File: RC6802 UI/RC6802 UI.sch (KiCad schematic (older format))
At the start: 71 parts, among them J1 TAPE, J2 RC6802_UI_Port, M1 Mounting, M2 Mounting, M3 Mounting, M4 Mounting, Q1 2N3904, Q2 2N3904, Q3 2N3904, Q4 2N3904, Q5 2N3904, SW1 RESET, SW10 D, SW11 2, SW12 6, SW13 A, SW14 E, SW15 3, SW16 7, SW17 B, SW18 F, SW19 LOAD, SW2 SST, SW3 Ø, SW4 4, SW5 8, SW6 C, SW7 1, SW8 5, SW9 9, U1 74LS374, U2 74LS00

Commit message: Assigned 7segment and tape footprints
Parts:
- added C3: 100nF, Capacitors_THT:C_Disc_D4.7mm_W2.5mm_P5.00mm, symbol C
- added SW20: STEP, symbol SW_SPDT
- AFF1, AFF2: footprint (none) -> Displays_7-Segment:7SegmentLED_LTS6760_LTS6780
- D1: footprint (none) -> LEDs:LED_D5.0mm
- D2, D3, D4: footprint (none) -> Diodes_THT:D_DO-35_SOD27_P7.62mm_Horizontal
- J1: footprint (none) -> TRS:Tayda_3.5mm_stereo_TRS_jack_A-853
- R1, R10, R11, R12, R13, R14, R15, R16, R17, R18, R19, R2, R20, R21, R22, R23, R24, R25, R26, R3, R4, R5, R6, R7, R8, R9: footprint (none) -> Resistors_THT:R_Axial_DIN0207_L6.3mm_D2.5mm_P10.16mm_Horizontal
- SW1, SW10, SW11, SW12, SW13, SW14, SW15, SW16, SW17, SW18, SW3, SW4, SW5, SW6, SW7, SW8, SW9: footprint (none) -> Buttons_Switches_THT:SW_PUSH_6mm
- SW19, SW2: footprint (none) -> Pin_Headers:Pin_Header_Straight_1x03_Pitch2.54mm
- U1: footprint (none) -> Housings_DIP:DIP-20_W7.62mm_Socket
- U2: footprint (none) -> Housings_DIP:DIP-14_W7.62mm_Socket
- renumbered C3 to C8
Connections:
- wire segments 233 -> 235
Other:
- note added: "Uses the same cable setup as found\non the ZX Spectrum +3, with EAR\nis data from tape to computer -\nMIC is data out to tape."

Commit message: UI board layout done
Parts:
- removed Q1, Q2: 2N3904, TO_SOT_Packages_THT:TO-92_Molded_Narrow, symbol 2N3904
- removed SW19: LOAD, Pin_Headers:Pin_Header_Straight_1x03_Pitch2.54mm, symbol SW_SPDT
- removed SW2: SST, Pin_Headers:Pin_Header_Straight_1x03_Pitch2.54mm, symbol SW_SPDT
- removed SW20: STEP, symbol SW_SPDT
- added J3: EXT_KEYPAD, Pin_Headers:Pin_Header_Angled_2x05_Pitch2.54mm, symbol Conn_02x05_Odd_Even
- added Q1, Q2: 2N3906, TO_SOT_Packages_THT:TO-92_Molded_Narrow, symbol 2N3906
- added R27, R29: 220, Resistors_THT:R_Axial_DIN0207_L6.3mm_D2.5mm_P10.16mm_Horizontal, symbol R
- added R28, R30: 1k, Resistors_THT:R_Axial_DIN0207_L6.3mm_D2.5mm_P10.16mm_Horizontal, symbol R
- added SW19: TAPE, DPDT_Switch:dpdt_switch, symbol SW_DPDT_x2
- added SW2: SW_SST, DPDT_Switch:dpdt_switch, symbol SW_DPDT_x2
- added SW20: STEP, DPDT_Switch:dpdt_switch, symbol SW_DPDT_x2
- added SW21: HW_SST, DPDT_Switch:dpdt_switch, symbol SW_DPDT_x2
- added U3: 74LS73, Housings_DIP:DIP-14_W7.62mm_Socket, symbol 74LS73
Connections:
- net labels added: E, ~HALT
- wire segments 235 -> 278
- no-connect marks 20 -> 31
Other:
- note added: "RC6802 Microchicken computer as explained in the book "22 Micro-computer projects:\nTo build, use and learn" by Daniel Metzger. UI board implements 7segment output, tape\ninput/output, single-step circuit and keypad.\n\nComponents for keypad (in favor of an external one), tape and the 74LS73 (for SST) can\nbe left out if not needed."
- note added: "Software SST is used by latching\nthe IRQ line permanently low."
- moved on the sheet: AFF1, AFF2, C1, C2, C3, C4, C5, C6, C7, C8, D1, D2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

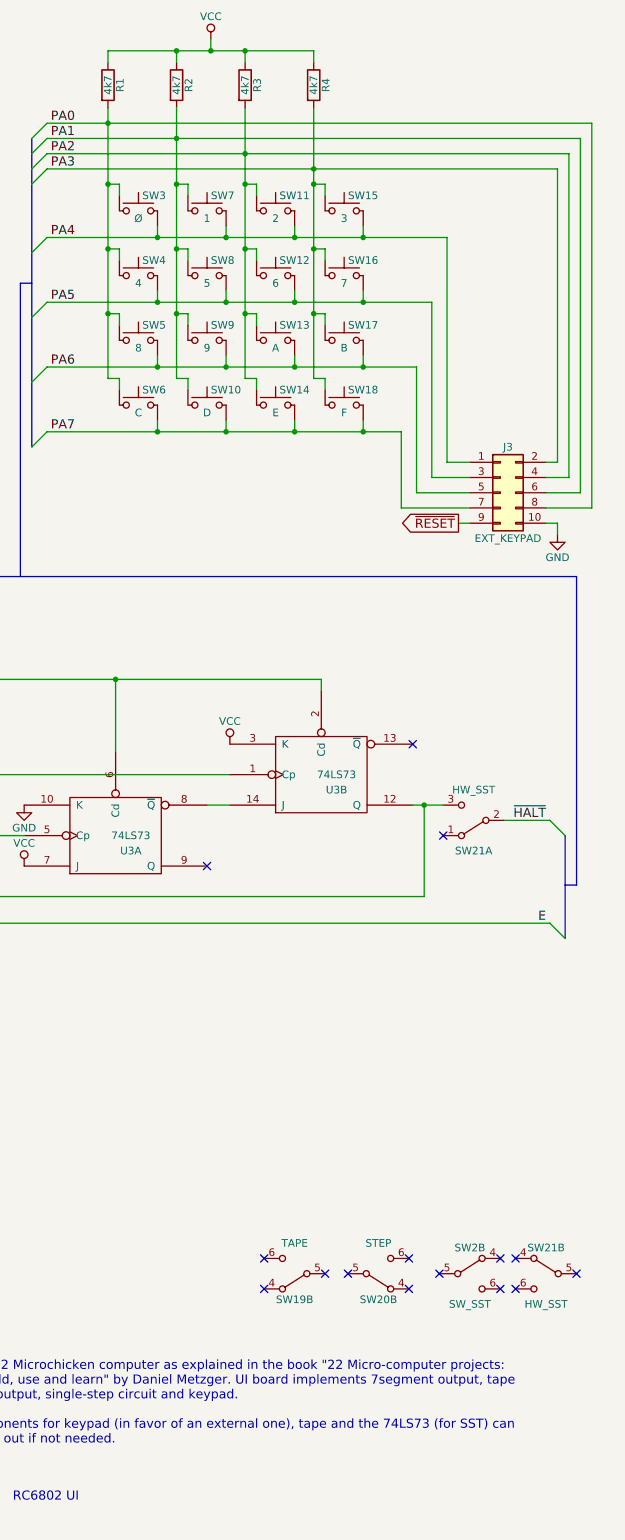
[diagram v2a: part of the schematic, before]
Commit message: Updated UI to change footprints
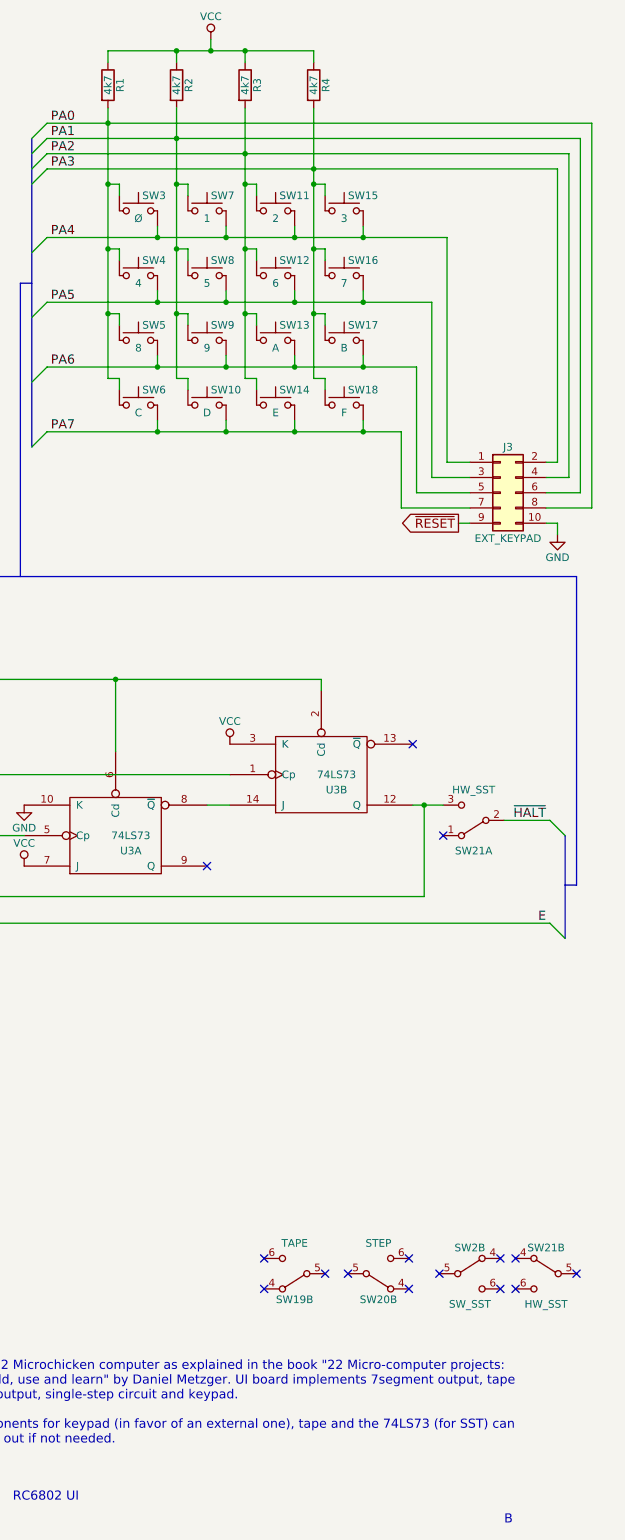
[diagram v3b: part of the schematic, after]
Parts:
- SW19, SW2, SW20, SW21: footprint DPDT_Switch:dpdt_switch -> DPDT_Switch:dpdt_switch_black
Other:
- note added: "B"
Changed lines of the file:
@@
 $EndComp
 $Comp
-L GND #PWR6
+L GND #PWR01
 U 1 1 5D65DEF6
 P 3325 1700
-F 0 "#PWR6" H 3325 1450 50  0001 C CNN
+F 0 "#PWR01" H 3325 1450 50  0001 C CNN
 F 1 "GND" H 3325 1550 50  0000 C CNN
 F 2 "" H 3325 1700 50  0001 C CNN
@@
 $EndComp
 $Comp
-L VCC #PWR1
+L VCC #PWR02
 U 1 1 5D65E216
 P 1825 1550
-F 0 "#PWR1" H 1825 1400 50  0001 C CNN
+F 0 "#PWR02" H 1825 1400 50  0001 C CNN
 F 1 "VCC" H 1825 1700 50  0000 C CNN
 F 2 "" H 1825 1550 50  0001 C CNN
@@
 $EndComp
 $Comp
-L GND #PWR19
+L GND #PWR03
 U 1 1 5D71E74B
 P 11475 10875
-F 0 "#PWR19" H 11475 10625 50  0001 C CNN
+F 0 "#PWR03" H 11475 10625 50  0001 C CNN
 F 1 "GND" H 11475 10725 50  0000 C CNN
 F 2 "" H 11475 10875 50  0001 C CNN
@@
 $EndComp
 $Comp
-L VCC #PWR18
+L VCC #PWR04
 U 1 1 5D72035A
 P 10875 10275
-F 0 "#PWR18" H 10875 10125 50  0001 C CNN
+F 0 "#PWR04" H 10875 10125 50  0001 C CNN
 F 1 "VCC" H 10875 10425 50  0000 C CNN
 F 2 "" H 10875 10275 50  0001 C CNN
@@
 $EndComp
 $Comp
-L GND #PWR5
+L GND #PWR05
 U 1 1 5D72A34D
 P 2925 3600
-F 0 "#PWR5" H 2925 3350 50  0001 C CNN
+F 0 "#PWR05" H 2925 3350 50  0001 C CNN
 F 1 "GND" H 2925 3450 50  0000 C CNN
 F 2 "" H 2925 3600 50  0001 C CNN
@@
 ~RESET
 $Comp
-L GND #PWR3
+L GND #PWR06
 U 1 1 5D840F7E
 P 2000 4450
-F 0 "#PWR3" H 2000 4200 50  0001 C CNN
+F 0 "#PWR06" H 2000 4200 50  0001 C CNN
 F 1 "GND" H 2000 4300 50  0000 C CNN
 F 2 "" H 2000 4450 50  0001 C CNN
@@
 NoConn ~ 2150 5100
 $Comp
-L GND #PWR4
+L GND #PWR07
 U 1 1 5D842BAE
 P 2000 4975
-F 0 "#PWR4" H 2000 4725 50  0001 C CNN
+F 0 "#PWR07" H 2000 4725 50  0001 C CNN
 F 1 "GND" H 2000 4825 50  0000 C CNN
 F 2 "" H 2000 4975 50  0001 C CNN
@@
 PA7
 $Comp
-L VCC #PWR22
+L VCC #PWR08
 U 1 1 5D84C6E3
 P 13475 1325
-F 0 "#PWR22" H 13475 1175 50  0001 C CNN
+F 0 "#PWR08" H 13475 1175 50  0001 C CNN
 F 1 "VCC" H 13475 1475 50  0000 C CNN
 F 2 "" H 13475 1325 50  0001 C CNN
@@
 $EndComp
 $Comp
-L GND #PWR2
+L GND #PWR09
 U 1 1 5D850423
 P 1825 9075
-F 0 "#PWR2" H 1825 8825 50  0001 C CNN
+F 0 "#PWR09" H 1825 8825 50  0001 C CNN
 F 1 "GND" H 1825 8925 50  0000 C CNN
 F 2 "" H 1825 9075 50  0001 C CNN
@@
 $EndComp
 $Comp
-L GND #PWR12
+L GND #PWR010
 U 1 1 5D861B67
 P 6850 4000
-F 0 "#PWR12" H 6850 3750 50  0001 C CNN
+F 0 "#PWR010" H 6850 3750 50  0001 C CNN
 F 1 "GND" H 6850 3850 50  0000 C CNN
 F 2 "" H 6850 4000 50  0001 C CNN
@@
 $EndComp
 $Comp
-L GND #PWR8
+L GND #PWR011
 U 1 1 5D86561F
 P 5825 4175
-F 0 "#PWR8" H 5825 3925 50  0001 C CNN
+F 0 "#PWR011" H 5825 3925 50  0001 C CNN
 F 1 "GND" H 5825 4025 50  0000 C CNN
 F 2 "" H 5825 4175 50  0001 C CNN
@@
 $EndComp
 $Comp
-L GND #PWR17
+L GND #PWR012
 U 1 1 5D8681F1
 P 10575 3000
-F 0 "#PWR17" H 10575 2750 50  0001 C CNN
+F 0 "#PWR012" H 10575 2750 50  0001 C CNN
 F 1 "GND" H 10575 2850 50  0000 C CNN
 F 2 "" H 10575 3000 50  0001 C CNN
@@
 $EndComp
 $Comp
-L VCC #PWR16
+L VCC #PWR013
 U 1 1 5D86AC5E
 P 10025 1675
-F 0 "#PWR16" H 10025 1525 50  0001 C CNN
+F 0 "#PWR013" H 10025 1525 50  0001 C CNN
 F 1 "VCC" H 10025 1825 50  0000 C CNN
 F 2 "" H 10025 1675 50  0001 C CNN
@@
 $EndComp
 $Comp
-L GND #PWR14
+L GND #PWR014
 U 1 1 5D872E9C
 P 7025 2825
-F 0 "#PWR14" H 7025 2575 50  0001 C CNN
+F 0 "#PWR014" H 7025 2575 50  0001 C CNN
 F 1 "GND" H 7025 2675 50  0000 C CNN
 F 2 "" H 7025 2825 50  0001 C CNN
@@
 $EndComp
 $Comp
-L GND #PWR11
+L GND #PWR015
 U 1 1 5D878DBF
 P 6100 2450
-F 0 "#PWR11" H 6100 2200 50  0001 C CNN
+F 0 "#PWR015" H 6100 2200 50  0001 C CNN
 F 1 "GND" H 6100 2300 50  0000 C CNN
 F 2 "" H 6100 2450 50  0001 C CNN
@@
 $EndComp
 $Comp
-L VCC #PWR13
+L VCC #PWR016
 U 1 1 5D87A6AC
 P 7025 1275
-F 0 "#PWR13" H 7025 1125 50  0001 C CNN
+F 0 "#PWR016" H 7025 1125 50  0001 C CNN
 F 1 "VCC" H 7025 1425 50  0000 C CNN
 F 2 "" H 7025 1275 50  0001 C CNN
@@
 $EndComp
 $Comp
-L VCC #PWR10
+L VCC #PWR017
 U 1 1 5D87AD7F
 P 6100 1275
-F 0 "#PWR10" H 6100 1125 50  0001 C CNN
+F 0 "#PWR017" H 6100 1125 50  0001 C CNN
 F 1 "VCC" H 6100 1425 50  0000 C CNN
 F 2 "" H 6100 1275 50  0001 C CNN
@@
 Uses the same cable setup as found\non the ZX Spectrum +3, with EAR\nis data from tape to computer -\nMIC is data out to tape.
 $Comp
-L GND #PWR15
+L GND #PWR018
 U 1 1 5D8923B4
 P 7925 6125
-F 0 "#PWR15" H 7925 5875 50  0001 C CNN
+F 0 "#PWR018" H 7925 5875 50  0001 C CNN
 F 1 "GND" H 7925 5975 50  0000 C CNN
 F 2 "" H 7925 6125 50  0001 C CNN
@@
 $EndComp
 $Comp
-L GND #PWR20
+L GND #PWR019
 U 1 1 5D85C3D7
 P 12250 6350
-F 0 "#PWR20" H 12250 6100 50  0001 C CNN
+F 0 "#PWR019" H 12250 6100 50  0001 C CNN
 F 1 "GND" H 12250 6200 50  0000 C CNN
 F 2 "" H 12250 6350 50  0001 C CNN
@@
 $EndComp
 $Comp
-L VCC #PWR23
+L VCC #PWR020
 U 1 1 5D85C9F0
 P 13600 5950
-F 0 "#PWR23" H 13600 5800 50  0001 C CNN
+F 0 "#PWR020" H 13600 5800 50  0001 C CNN
 F 1 "VCC" H 13600 6100 50  0000 C CNN
 F 2 "" H 13600 5950 50  0001 C CNN
@@
 NoConn ~ 14800 5950
 $Comp
-L VCC #PWR21
+L VCC #PWR021
 U 1 1 5D85EA21
 P 12250 6750
-F 0 "#PWR21" H 12250 6600 50  0001 C CNN
+F 0 "#PWR021" H 12250 6600 50  0001 C CNN
 F 1 "VCC" H 12250 6900 50  0000 C CNN
 F 2 "" H 12250 6750 50  0001 C CNN
@@
 F 0 "SW21" H 15200 6650 50  0000 C CNN
 F 1 "HW_SST" H 15200 6250 50  0000 C CNN
-F 2 "DPDT_Switch:dpdt_switch" H 15200 6450 50  0001 C CNN
+F 2 "DPDT_Switch:dpdt_switch_black" H 15200 6450 50  0001 C CNN
 F 3 "" H 15200 6450 50  0001 C CNN
 	1    15200 6450
@@
 F 0 "SW21" H 15675 9595 50  0000 C CNN
 F 1 "HW_SST" H 15675 9225 50  0000 C CNN
-F 2 "DPDT_Switch:dpdt_switch" H 15675 9425 50  0001 C CNN
+F 2 "DPDT_Switch:dpdt_switch_black" H 15675 9425 50  0001 C CNN
 F 3 "" H 15675 9425 50  0001 C CNN
 	2    15675 9425
@@
 F 0 "SW2" H 2350 5170 50  0000 C CNN
 F 1 "SW_SST" H 2350 4800 50  0000 C CNN
-F 2 "DPDT_Switch:dpdt_switch" H 2350 5000 50  0001 C CNN
+F 2 "DPDT_Switch:dpdt_switch_black" H 2350 5000 50  0001 C CNN
 F 3 "" H 2350 5000 50  0001 C CNN
 	1    2350 5000
@@
 F 0 "SW2" H 15175 9595 50  0000 C CNN
 F 1 "SW_SST" H 15175 9225 50  0000 C CNN
-F 2 "DPDT_Switch:dpdt_switch" H 15175 9425 50  0001 C CNN
+F 2 "DPDT_Switch:dpdt_switch_black" H 15175 9425 50  0001 C CNN
 F 3 "" H 15175 9425 50  0001 C CNN
 	2    15175 9425
@@
 F 0 "SW20" H 8200 6220 50  0000 C CNN
 F 1 "STEP" H 8200 5850 50  0000 C CNN
-F 2 "DPDT_Switch:dpdt_switch" H 8200 6050 50  0001 C CNN
+F 2 "DPDT_Switch:dpdt_switch_black" H 8200 6050 50  0001 C CNN
 F 3 "" H 8200 6050 50  0001 C CNN
 	1    8200 6050
@@
 F 0 "SW20" H 14575 9595 50  0000 C CNN
 F 1 "STEP" H 14575 9225 50  0000 C CNN
-F 2 "DPDT_Switch:dpdt_switch" H 14575 9425 50  0001 C CNN
+F 2 "DPDT_Switch:dpdt_switch_black" H 14575 9425 50  0001 C CNN
 F 3 "" H 14575 9425 50  0001 C CNN
 	2    14575 9425
@@
 F 0 "SW19" H 5525 2320 50  0000 C CNN
 F 1 "TAPE" H 5525 1950 50  0000 C CNN
-F 2 "DPDT_Switch:dpdt_switch" H 5525 2150 50  0001 C CNN
+F 2 "DPDT_Switch:dpdt_switch_black" H 5525 2150 50  0001 C CNN
 F 3 "" H 5525 2150 50  0001 C CNN
 	1    5525 2150
@@
 F 0 "SW19" H 14025 9595 50  0000 C CNN
 F 1 "TAPE" H 14025 9225 50  0000 C CNN
-F 2 "DPDT_Switch:dpdt_switch" H 14025 9425 50  0001 C CNN
+F 2 "DPDT_Switch:dpdt_switch_black" H 14025 9425 50  0001 C CNN
 F 3 "" H 14025 9425 50  0001 C CNN
 	2    14025 9425
@@
 $EndComp
 $Comp
-L VCC #PWR9
+L VCC #PWR022
 U 1 1 5D8C1B27
 P 6025 8400
-F 0 "#PWR9" H 6025 8250 50  0001 C CNN
+F 0 "#PWR022" H 6025 8250 50  0001 C CNN
 F 1 "VCC" H 6025 8550 50  0000 C CNN
 F 2 "" H 6025 8400 50  0001 C CNN
@@
 	13325 3625 13325 3550
 Wire Wire Line
-	13250 3550 13325 3550
+	13325 3550 13250 3550
 Wire Wire Line
 	12875 3625 12875 3550
 Wire Wire Line
-	12800 3550 12875 3550
+	12875 3550 12800 3550
 Wire Wire Line
 	13775 3625 13775 3550
 Wire Wire Line
-	13700 3550 13775 3550
+	13775 3550 13700 3550
 Wire Wire Line
 	14225 3625 14225 3550
 Wire Wire Line
-	14150 3550 14225 3550
+	14225 3550 14150 3550
 Wire Wire Line
 	13575 3900 13575 3825
@@
 	14025 3900 14025 3825
 Wire Wire Line
-	12800 1775 12800 3550
+	12800 3550 12800 1775
 Connection ~ 12800 3125
 Connection ~ 12800 2700
 Wire Wire Line
-	13250 1775 13250 3550
+	13250 3550 13250 1775
 Connection ~ 13250 2700
 Connection ~ 13250 3125
 Wire Wire Line
-	13700 1775 13700 3550
+	13700 3550 13700 1775
 Connection ~ 13700 3125
 Connection ~ 13700 2700
 Wire Wire Line
-	14150 1775 14150 3550
+	14150 3550 14150 1775
 Connection ~ 14150 2700
 Connection ~ 14150 3125
@@
 $EndComp
 $Comp
-L VCC #PWR7
+L VCC #PWR023
 U 1 1 5D8C7C19
 P 5625 7250
-F 0 "#PWR7" H 5625 7100 50  0001 C CNN
+F 0 "#PWR023" H 5625 7100 50  0001 C CNN
 F 1 "VCC" H 5625 7400 50  0000 C CNN
 F 2 "" H 5625 7250 50  0001 C CNN
@@
 	15100 4500 15175 4500
 $Comp
-L GND #PWR24
+L GND #PWR024
 U 1 1 5D8F6D89
 P 15750 4575
-F 0 "#PWR24" H 15750 4325 50  0001 C CNN
+F 0 "#PWR024" H 15750 4325 50  0001 C CNN
 F 1 "GND" H 15750 4425 50  0000 C CNN
 F 2 "" H 15750 4575 50  0001 C CNN
@@
 Wire Bus Line
 	1450 8550 1450 2575
+Text Notes 15400 11075 0    60   ~ 0
+B
 $EndSCHEMATC

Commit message: Revision B build
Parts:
- SW2: value SW_SST -> ~IRQ
- SW21: value HW_SST -> SST
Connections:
- net GND: now also SW2.3 (C); no longer SW2.1 (A)
- net PB7: now also SW19.3 (C); no longer SW19.1 (A)
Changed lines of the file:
@@
 Text GLabel 2625 5000 2    60   Output ~ 0
 ~SST
-NoConn ~ 2150 5100
+NoConn ~ 2150 4900
 $Comp
 L GND #PWR07
 U 1 1 5D842BAE
-P 2000 4975
-F 0 "#PWR07" H 2000 4725 50  0001 C CNN
-F 1 "GND" H 2000 4825 50  0000 C CNN
-F 2 "" H 2000 4975 50  0001 C CNN
-F 3 "" H 2000 4975 50  0001 C CNN
-	1    2000 4975
+P 2000 5175
+F 0 "#PWR07" H 2000 4925 50  0001 C CNN
+F 1 "GND" H 2000 5025 50  0000 C CNN
+F 2 "" H 2000 5175 50  0001 C CNN
+F 3 "" H 2000 5175 50  0001 C CNN
+	1    2000 5175
 	1    0    0    -1
 $EndComp
@@
 Entry Wire Line
 	15700 7125 15800 7225
-Text Notes 1725 5450 0    60   ~ 0
+Text Notes 1725 5600 0    60   ~ 0
 Software SST is used by latching\nthe IRQ line permanently low.
 NoConn ~ 15000 6550
@@
 P 15200 6450
 F 0 "SW21" H 15200 6650 50  0000 C CNN
-F 1 "HW_SST" H 15200 6250 50  0000 C CNN
+F 1 "SST" H 15200 6250 50  0000 C CNN
 F 2 "DPDT_Switch:dpdt_switch_black" H 15200 6450 50  0001 C CNN
 F 3 "" H 15200 6450 50  0001 C CNN
@@
 P 15675 9425
 F 0 "SW21" H 15675 9595 50  0000 C CNN
-F 1 "HW_SST" H 15675 9225 50  0000 C CNN
+F 1 "SST" H 15675 9225 50  0000 C CNN
 F 2 "DPDT_Switch:dpdt_switch_black" H 15675 9425 50  0001 C CNN
 F 3 "" H 15675 9425 50  0001 C CNN
@@
 P 2350 5000
 F 0 "SW2" H 2350 5170 50  0000 C CNN
-F 1 "SW_SST" H 2350 4800 50  0000 C CNN
+F 1 "~IRQ" H 2350 4800 50  0000 C CNN
 F 2 "DPDT_Switch:dpdt_switch_black" H 2350 5000 50  0001 C CNN
 F 3 "" H 2350 5000 50  0001 C CNN
@@
 P 15175 9425
 F 0 "SW2" H 15175 9595 50  0000 C CNN
-F 1 "SW_SST" H 15175 9225 50  0000 C CNN
+F 1 "~IRQ" H 15175 9225 50  0000 C CNN
 F 2 "DPDT_Switch:dpdt_switch_black" H 15175 9425 50  0001 C CNN
 F 3 "" H 15175 9425 50  0001 C CNN
@@
 F 3 "" H 5525 2150 50  0001 C CNN
 	1    5525 2150
-	0    1    1    0
+	0    -1   1    0
 $EndComp
 $Comp
@@
 	2625 5000 2550 5000
 Wire Wire Line
-	2150 4900 2000 4900
-Wire Wire Line
-	2000 4900 2000 4975
+	2150 5100 2000 5100
+Wire Wire Line
+	2000 5100 2000 5175
 Wire Wire Line
 	2000 4450 2000 4375

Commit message: IC-Tester original code
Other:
- note added: "$2000"
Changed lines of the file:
@@
 Text Notes 15400 11075 0    60   ~ 0
 B
+Text Notes 2450 9150 0    60   ~ 0
+$2000
 $EndSCHEMATC
